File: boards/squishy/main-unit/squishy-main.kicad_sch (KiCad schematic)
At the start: 89 parts, among them J1 Conn_01x02, J3 MEM2061-01-188-00-A, J42 SU SWD, J7 SCSI PHY Mezz, J8 FLASH, J8 TRIGGER, SW2 DFU, U1 LFE5UM5G-45F-8BG381C, U18 IS66WVS4M8BLL, U19 HyperRAM, U2 GD25Q64EWIGR, U24 74AHC1G02, U6 ATSAMD09D14A-M, X1 48MHz, X3 100MHz

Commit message: squishy: main: started populating part links prior to going through each part (other than passives) and validating their footprints
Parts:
- C1, C57: OC_DIGIKEY (none) -> 399-C0402C103K3RAC7867DKR-ND; URL_DIGIKEY (none) -> https://www.digikey.com/short/n9t0571b
- C12, C47, C7: OC_DIGIKEY (none) -> 399-C0603C104M5RAC7867DKR-ND; URL_DIGIKEY (none) -> https://www.digikey.com/short/8nqzrr4b
- C13, C14, C5: OC_DIGIKEY (none) -> 587-2400-6-ND; URL_DIGIKEY (none) -> https://www.digikey.com/short/83w49wnp
- D10: OC_DIGIKEY (none) -> SMLEN3WBC8W1DKR-ND; URL_DIGIKEY (none) -> https://www.digikey.com/short/c3th3r99
- D12, D8: OC_DIGIKEY (none) -> 732-4966-6-ND; URL_DIGIKEY (none) -> https://www.digikey.com/short/ddpjpwr7
- D15: OC_DIGIKEY (none) -> 732-4978-6-ND; URL_DIGIKEY (none) -> https://www.digikey.com/short/whr1znbf
- D16: OC_DIGIKEY (none) -> 732-4980-6-ND; URL_DIGIKEY (none) -> https://www.digikey.com/short/h8jf77w9
- D17: URL_DIGIKEY (none) -> https://www.digikey.com/short/dbc27874
- J3: OC_DIGIKEY (none) -> 2073-MEM2061-01-188-00-ADKR-ND; URL_DIGIKEY (none) -> https://www.digikey.com/short/pnmr2wrw
- J42, J8: MPN FTSH-105-01-L-DV-K-TR -> FTSH-105-01-L-DV-K-P-TR; OC_DIGIKEY (none) -> 612-FTSH-105-01-L-DV-K-P-TRDKR-ND; URL_DIGIKEY (none) -> https://www.digikey.com/short/mw4tvzw7
- J7: URL_DIGIKEY (none) -> https://www.digikey.com/short/rh8jztt0
- J8: OC_DIGIKEY (none) -> WM5536-ND; URL_DIGIKEY (none) -> https://www.digikey.com/short/ch5zfdz7

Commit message: squishy: main: added the last of the Digikey order codes and URLs, some parts are not available at DigiKey and others are out of stock with long lead times, need to find alternatives. While also there are some that don't come in digireel so no idea what to do there
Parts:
- R10, R12, R37, R38, R39, R49, R58, R71, R72, R73, R74: OC_DIGIKEY (none) -> 541-4.70KHDKR-ND; URL_DIGIKEY (none) -> https://www.digikey.com/short/f3fq37nd
- R11: OC_DIGIKEY (none) -> 541-1.00MHDKR-ND; URL_DIGIKEY (none) -> https://www.digikey.com/short/18qqp0zw
- R12: OC_DIGIKEY (none) -> 541-0.0JDKR-ND; Tolerance (none) -> 1/4W; URL_DIGIKEY (none) -> https://www.digikey.com/short/qmj7b2hp
- R12: OC_DIGIKEY (none) -> 541-1.00KHDKR-ND; URL_DIGIKEY (none) -> https://www.digikey.com/short/dw9cq7z3
- R19, R20, R21, R22, R23: OC_DIGIKEY (none) -> 541-2.20KHDKR-ND; URL_DIGIKEY (none) -> https://www.digikey.com/short/bnh9rvr0
- R19, R20: OC_DIGIKEY (none) -> 541-100KHDKR-ND; URL_DIGIKEY (none) -> https://www.digikey.com/short/5n1ztv42
- R25, R3, R36, R54, R60, R64, R67, R68, R69, R70: OC_DIGIKEY (none) -> 541-10.0KHDKR-ND; URL_DIGIKEY (none) -> https://www.digikey.com/short/478v2810
- R37: OC_DIGIKEY (none) -> CAY16-4701F4LFDKR-ND; URL_DIGIKEY (none) -> https://www.digikey.com/short/zvwmjpcm
- R37, R66: OC_DIGIKEY (none) -> CAY16-103J4LFDKR-ND; URL_DIGIKEY (none) -> https://www.digikey.com/short/91vhpmq2
- R5: OC_DIGIKEY (none) -> 541-100LDKR-ND; URL_DIGIKEY (none) -> https://www.digikey.com/short/v1307zwt
- SW2: OC_DIGIKEY (none) -> SW1143DKR-ND; URL_DIGIKEY (none) -> https://www.digikey.com/short/vvt30n4j
- U1: OC_DIGIKEY (none) -> 220-2107-ND; URL_DIGIKEY (none) -> https://www.digikey.com/short/f34t0pr0
- U18, U19: OC_DIGIKEY (none) -> 448-S80KS5122GABHI020-ND; URL_DIGIKEY (none) -> https://www.digikey.com/short/rwv27n90
- U18: OC_DIGIKEY (none) -> 706-IS66WVS4M8BLL-104NLI-ND; URL_DIGIKEY (none) -> https://www.digikey.com/short/29w7cnhb
- U2: OC_DIGIKEY (none) -> 1970-GD25Q64EWIGRDKR-ND; URL_DIGIKEY (none) -> https://www.digikey.com/short/j44d557m
- U24: OC_DIGIKEY (none) -> 1727-3258-6-ND; URL_DIGIKEY (none) -> https://www.digikey.com/short/pb7573pr
- U6: OC_DIGIKEY (none) -> ATSAMD09D14A-MUTDKR-ND; URL_DIGIKEY (none) -> https://www.digikey.com/short/7423wbjd
- X1: OC_DIGIKEY (none) -> 535-ASE-48.000MHZ-L-C-TDKR-ND; URL_DIGIKEY (none) -> https://www.digikey.com/short/pmhjnqwd
- X3: OC_DIGIKEY (none) -> 535-AK3ADDF1-100.000T3DKR-ND; URL_DIGIKEY (none) -> https://www.digikey.com/short/5r299tzp

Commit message: squishy: main: BoM cleanup and alternative part selection for the ones which were out of stock
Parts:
- D11, D9: OC_DIGIKEY (none) -> OSK40603C1E; URL_DIGIKEY (none) -> https://www.tme.com/ux/en-us/details/osk40603c1e/smd-colour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
- D17: OC_DIGIKEY (none) -> 18-SP3205-01ETGCT-ND
- J7: OC_DIGIKEY (none) -> 609-5457-1-ND
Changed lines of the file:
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@@
 			)
 		)
-		(property "OC_DIGIKEY" ""
+		(property "OC_DIGIKEY" "OSK40603C1E"
 			(at 118.11 40.64 0)
 			(effects
@@
 			)
 		)
-		(property "URL_DIGIKEY" ""
+		(property "URL_DIGIKEY" "https://www.tme.com/ux/en-us/details/osk40603c1e/smd-colour-leds/optosupply/"
 			(at 118.11 40.64 0)
 			(effects
@@
 			)
 		)
-		(property "OC_DIGIKEY" ""
+		(property "OC_DIGIKEY" "OSK40603C1E"
 			(at 128.27 40.64 0)
 			(effects
@@
 			)
 		)
-		(property "URL_DIGIKEY" ""
+		(property "URL_DIGIKEY" "https://www.tme.com/ux/en-us/details/osk40603c1e/smd-colour-leds/optosupply/"
 			(at 128.27 40.64 0)
 			(effects
@@
 			)
 		)
-		(property "OC_DIGIKEY" ""
+		(property "OC_DIGIKEY" "18-SP3205-01ETGCT-ND"
 			(at 69.85 30.48 0)
 			(effects
@@
 			)
 		)
-		(property "OC_DIGIKEY" ""
+		(property "OC_DIGIKEY" "609-5457-1-ND"
 			(at 367.03 158.75 0)
 			(effects

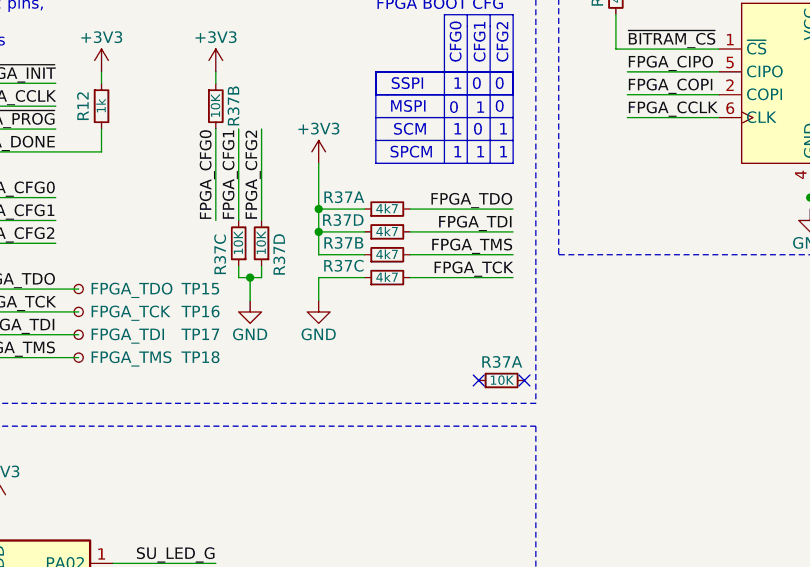
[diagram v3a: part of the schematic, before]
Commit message: squishy: main: Replaced the single 4k7 resistor network with 4 dedicated resistors to reduce BOM count
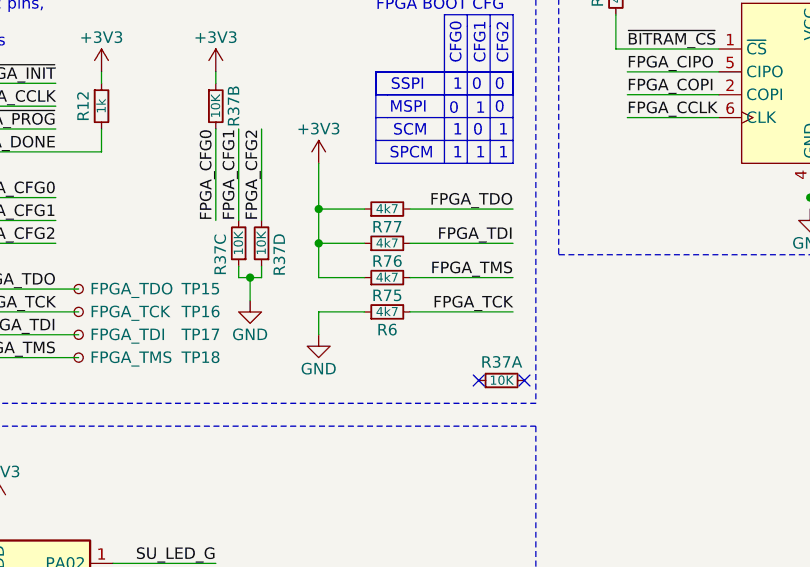
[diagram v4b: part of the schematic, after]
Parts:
- removed R37: 4k7, rhais_rcl:R0603_Array_Concave_4, symbol DX-MON:pkl_R4_Small
- added R6, R75, R76, R77: 4k7, rhais_rcl:R0603, symbol Device:R_Small
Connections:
- net +3V3: now also R75.1, R76.1, R77.1
- net FPGA_TCK: now also R6.2
- net FPGA_TDI: now also R76.2
- net FPGA_TDO: now also R77.2
- net FPGA_TMS: now also R75.2
- net GND: now also R6.1

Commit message: squishy: main: updated part fields to be more generic
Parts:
- C1, C57: OC_DIGIKEY 399-C0402C103K3RAC7867DKR-ND -> (none); SUPPLIER (none) -> DigiKey; SUPPLIER_OC (none) -> 399-C0402C103K3RAC7867DKR-ND; SUPPLIER_URL (none) -> https://www.digikey.com/short/n9t0571b; URL_DIGIKEY https://www.digikey.com/short/n9t0571b -> (none)
- C12, C47, C7: OC_DIGIKEY 399-C0603C104M5RAC7867DKR-ND -> (none); SUPPLIER (none) -> DigiKey; SUPPLIER_OC (none) -> 399-C0603C104M5RAC7867DKR-ND; SUPPLIER_URL (none) -> https://www.digikey.com/short/8nqzrr4b; URL_DIGIKEY https://www.digikey.com/short/8nqzrr4b -> (none)
- C13, C14, C5: OC_DIGIKEY 587-2400-6-ND -> (none); SUPPLIER (none) -> DigiKey; SUPPLIER_OC (none) -> 587-2400-6-ND; SUPPLIER_URL (none) -> https://www.digikey.com/short/83w49wnp; URL_DIGIKEY https://www.digikey.com/short/83w49wnp -> (none)
- D10: OC_DIGIKEY SMLEN3WBC8W1DKR-ND -> (none); SUPPLIER (none) -> DigiKey; SUPPLIER_OC (none) -> SMLEN3WBC8W1DKR-ND; SUPPLIER_URL (none) -> https://www.digikey.com/short/c3th3r99; URL_DIGIKEY https://www.digikey.com/short/c3th3r99 -> (none)
- D11, D9: OC_DIGIKEY OSK40603C1E -> (none); SUPPLIER (none) -> TME; SUPPLIER_OC (none) -> OSK40603C1E; SUPPLIER_URL (none) -> https://www.tme.com/ux/en-us/details/osk40603c1e/smd-colour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; URL_DIGIKEY https://www.tme.com/ux/en-us/details/osk40603c1e/smd-colour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 -> (none)
- D12, D8: OC_DIGIKEY 732-4966-6-ND -> (none); SUPPLIER (none) -> DigiKey; SUPPLIER_OC (none) -> 732-4966-6-ND; SUPPLIER_URL (none) -> https://www.digikey.com/short/ddpjpwr7; URL_DIGIKEY https://www.digikey.com/short/ddpjpwr7 -> (none)
- D15: OC_DIGIKEY 732-4978-6-ND -> (none); SUPPLIER (none) -> DigiKey; SUPPLIER_OC (none) -> 732-4978-6-ND; SUPPLIER_URL (none) -> https://www.digikey.com/short/whr1znbf; URL_DIGIKEY https://www.digikey.com/short/whr1znbf -> (none)
- D16: OC_DIGIKEY 732-4980-6-ND -> (none); SUPPLIER (none) -> DigiKey; SUPPLIER_OC (none) -> 732-4980-6-ND; SUPPLIER_URL (none) -> https://www.digikey.com/short/h8jf77w9; URL_DIGIKEY https://www.digikey.com/short/h8jf77w9 -> (none)
- D17: OC_DIGIKEY 18-SP3205-01ETGCT-ND -> (none); SUPPLIER (none) -> DigiKey; SUPPLIER_OC (none) -> 18-SP3205-01ETGCT-ND; SUPPLIER_URL (none) -> https://www.digikey.com/short/dbc27874; URL_DIGIKEY https://www.digikey.com/short/dbc27874 -> (none)
- J3: OC_DIGIKEY 2073-MEM2061-01-188-00-ADKR-ND -> (none); SUPPLIER (none) -> DigiKey; SUPPLIER_OC (none) -> 2073-MEM2061-01-188-00-ADKR-ND; SUPPLIER_URL (none) -> https://www.digikey.com/short/pnmr2wrw; URL_DIGIKEY https://www.digikey.com/short/pnmr2wrw -> (none)
- J42, J8: OC_DIGIKEY 612-FTSH-105-01-L-DV-K-P-TRDKR-ND -> (none); SUPPLIER_OC (none) -> 612-FTSH-105-01-L-DV-K-P-TRDKR-ND; SUPPLIER_URL (none) -> https://www.digikey.com/short/mw4tvzw7; URL_DIGIKEY https://www.digikey.com/short/mw4tvzw7 -> (none)
- J7: OC_DIGIKEY 609-5457-1-ND -> (none); SUPPLIER (none) -> DigiKey; SUPPLIER_OC (none) -> 609-5457-1-ND; SUPPLIER_URL (none) -> https://www.digikey.com/short/rh8jztt0; URL_DIGIKEY https://www.digikey.com/short/rh8jztt0 -> (none)
- J8: OC_DIGIKEY WM5536-ND -> (none); SUPPLIER_OC (none) -> WM5536-ND; SUPPLIER_URL (none) -> https://www.digikey.com/short/ch5zfdz7; URL_DIGIKEY https://www.digikey.com/short/ch5zfdz7 -> (none)
- R10, R12, R37, R38, R39, R49, R58, R6, R71, R72, R73, R74, R75, R76, R77: OC_DIGIKEY 541-4.70KHDKR-ND -> (none); SUPPLIER (none) -> DigiKey; SUPPLIER_OC (none) -> 541-4.70KHDKR-ND; SUPPLIER_URL (none) -> https://www.digikey.com/short/f3fq37nd; URL_DIGIKEY https://www.digikey.com/short/f3fq37nd -> (none)
- R11: OC_DIGIKEY 541-1.00MHDKR-ND -> (none); SUPPLIER (none) -> DigiKey; SUPPLIER_OC (none) -> 541-1.00MHDKR-ND; SUPPLIER_URL (none) -> https://www.digikey.com/short/18qqp0zw; URL_DIGIKEY https://www.digikey.com/short/18qqp0zw -> (none)
- R12: OC_DIGIKEY 541-0.0JDKR-ND -> (none); SUPPLIER (none) -> DigiKey; SUPPLIER_OC (none) -> 541-0.0JDKR-ND; SUPPLIER_URL (none) -> https://www.digikey.com/short/qmj7b2hp; URL_DIGIKEY https://www.digikey.com/short/qmj7b2hp -> (none)
- R12: OC_DIGIKEY 541-1.00KHDKR-ND -> (none); SUPPLIER (none) -> DigiKey; SUPPLIER_OC (none) -> 541-1.00KHDKR-ND; SUPPLIER_URL (none) -> https://www.digikey.com/short/dw9cq7z3; URL_DIGIKEY https://www.digikey.com/short/dw9cq7z3 -> (none)
- R19, R20, R21, R22, R23: OC_DIGIKEY 541-2.20KHDKR-ND -> (none); SUPPLIER (none) -> DigiKey; SUPPLIER_OC (none) -> 541-2.20KHDKR-ND; SUPPLIER_URL (none) -> https://www.digikey.com/short/bnh9rvr0; URL_DIGIKEY https://www.digikey.com/short/bnh9rvr0 -> (none)
- R19, R20: OC_DIGIKEY 541-100KHDKR-ND -> (none); SUPPLIER (none) -> DigiKey; SUPPLIER_OC (none) -> 541-100KHDKR-ND; SUPPLIER_URL (none) -> https://www.digikey.com/short/5n1ztv42; URL_DIGIKEY https://www.digikey.com/short/5n1ztv42 -> (none)
- R25, R3, R36, R54, R60, R64, R67, R68, R69, R70: OC_DIGIKEY 541-10.0KHDKR-ND -> (none); SUPPLIER (none) -> DigiKey; SUPPLIER_OC (none) -> 541-10.0KHDKR-ND; SUPPLIER_URL (none) -> https://www.digikey.com/short/478v2810; URL_DIGIKEY https://www.digikey.com/short/478v2810 -> (none)
- R37, R66: OC_DIGIKEY CAY16-103J4LFDKR-ND -> (none); SUPPLIER (none) -> DigiKey; SUPPLIER_OC (none) -> CAY16-103J4LFDKR-ND; SUPPLIER_URL (none) -> https://www.digikey.com/short/91vhpmq2; URL_DIGIKEY https://www.digikey.com/short/91vhpmq2 -> (none)
- R5: OC_DIGIKEY 541-100LDKR-ND -> (none); SUPPLIER (none) -> DigiKey; SUPPLIER_OC (none) -> 541-100LDKR-ND; SUPPLIER_URL (none) -> https://www.digikey.com/short/v1307zwt; URL_DIGIKEY https://www.digikey.com/short/v1307zwt -> (none)
- SW2: OC_DIGIKEY SW1143DKR-ND -> (none); SUPPLIER (none) -> DigiKey; SUPPLIER_OC (none) -> SW1143DKR-ND; SUPPLIER_URL (none) -> https://www.digikey.com/short/vvt30n4j; URL_DIGIKEY https://www.digikey.com/short/vvt30n4j -> (none)
- U1: OC_DIGIKEY 220-2107-ND -> (none); SUPPLIER (none) -> DigiKey; SUPPLIER_OC (none) -> 220-2107-ND; SUPPLIER_URL (none) -> https://www.digikey.com/short/f34t0pr0; URL_DIGIKEY https://www.digikey.com/short/f34t0pr0 -> (none)
- U18, U19: OC_DIGIKEY 448-S80KS5122GABHI020-ND -> (none); SUPPLIER (none) -> DigiKey; SUPPLIER_OC (none) -> 448-S80KS5122GABHI020-ND; SUPPLIER_URL (none) -> https://www.digikey.com/short/rwv27n90; URL_DIGIKEY https://www.digikey.com/short/rwv27n90 -> (none)
- U18: OC_DIGIKEY 706-IS66WVS4M8BLL-104NLI-ND -> (none); SUPPLIER (none) -> DigiKey; SUPPLIER_OC (none) -> 706-IS66WVS4M8BLL-104NLI-ND; SUPPLIER_URL (none) -> https://www.digikey.com/short/29w7cnhb; URL_DIGIKEY https://www.digikey.com/short/29w7cnhb -> (none)
- U2: OC_DIGIKEY 1970-GD25Q64EWIGRDKR-ND -> (none); SUPPLIER (none) -> DigiKey; SUPPLIER_OC (none) -> 1970-GD25Q64EWIGRDKR-ND; SUPPLIER_URL (none) -> https://www.digikey.com/short/j44d557m; URL_DIGIKEY https://www.digikey.com/short/j44d557m -> (none)
- U24: OC_DIGIKEY 1727-3258-6-ND -> (none); SUPPLIER (none) -> DigiKey; SUPPLIER_OC (none) -> 1727-3258-6-ND; SUPPLIER_URL (none) -> https://www.digikey.com/short/pb7573pr; URL_DIGIKEY https://www.digikey.com/short/pb7573pr -> (none)
- U6: OC_DIGIKEY ATSAMD09D14A-MUTDKR-ND -> (none); SUPPLIER (none) -> DigiKey; SUPPLIER_OC (none) -> ATSAMD09D14A-MUTDKR-ND; SUPPLIER_URL (none) -> https://www.digikey.com/short/7423wbjd; URL_DIGIKEY https://www.digikey.com/short/7423wbjd -> (none)
- X1: OC_DIGIKEY 535-ASE-48.000MHZ-L-C-TDKR-ND -> (none); SUPPLIER (none) -> DigiKey; SUPPLIER_OC (none) -> 535-ASE-48.000MHZ-L-C-TDKR-ND; SUPPLIER_URL (none) -> https://www.digikey.com/short/pmhjnqwd; URL_DIGIKEY https://www.digikey.com/short/pmhjnqwd -> (none)
- X3: OC_DIGIKEY 535-AK3ADDF1-100.000T3DKR-ND -> (none); SUPPLIER (none) -> DigiKey; SUPPLIER_OC (none) -> 535-AK3ADDF1-100.000T3DKR-ND; SUPPLIER_URL (none) -> https://www.digikey.com/short/5r299tzp; URL_DIGIKEY https://www.digikey.com/short/5r299tzp -> (none)

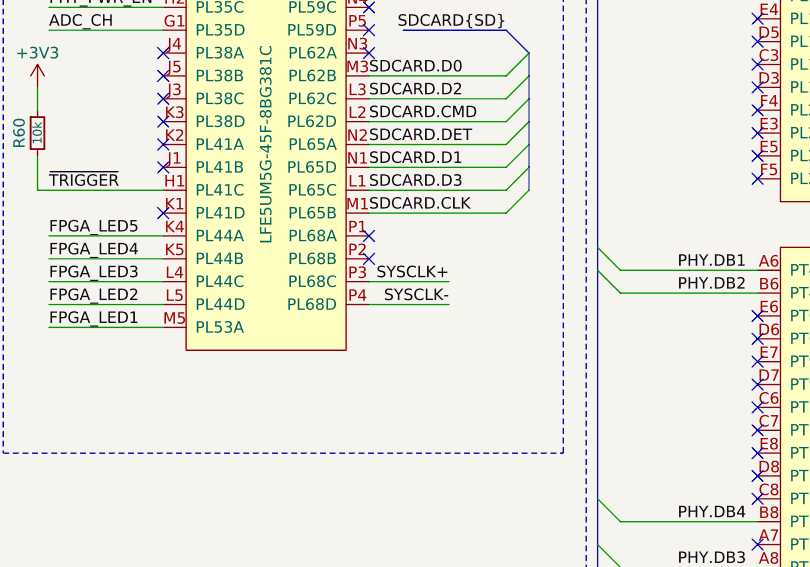
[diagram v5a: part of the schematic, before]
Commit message: squishy: main: fixed the pinout of the 100MHz and 200MHz LVDS oscillators, had to swap CLK+ and CLK- but because they're LVDS it shouldn't matter:tm:
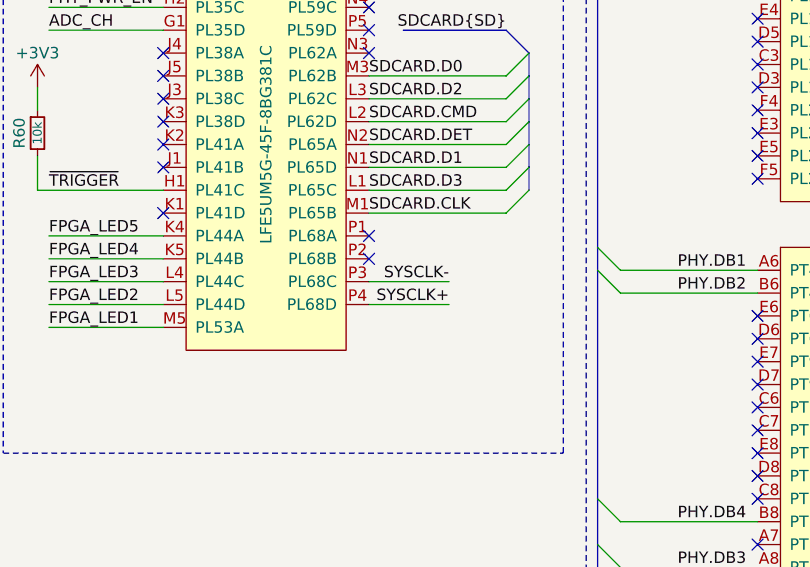
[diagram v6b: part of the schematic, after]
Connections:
- net SYSCLK+: now also U1.P4 (PL68D); no longer U1.P3 (PL68C)
- net SYSCLK-: now also U1.P3 (PL68C); no longer U1.P4 (PL68D)
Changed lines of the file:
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@@
 	(wire
 		(pts
-			(xy 241.3 146.05) (xy 250.19 146.05)
+			(xy 241.3 143.51) (xy 250.19 143.51)
 		)
 		(stroke
@@
 	(wire
 		(pts
-			(xy 241.3 143.51) (xy 250.19 143.51)
+			(xy 241.3 146.05) (xy 250.19 146.05)
 		)
 		(stroke
@@
 	)
 	(label "SYSCLK+"
-		(at 250.19 143.51 180)
+		(at 250.19 146.05 180)
 		(fields_autoplaced yes)
 		(effects
@@
 	)
 	(label "SYSCLK-"
-		(at 250.19 146.05 180)
+		(at 250.19 143.51 180)
 		(fields_autoplaced yes)
 		(effects

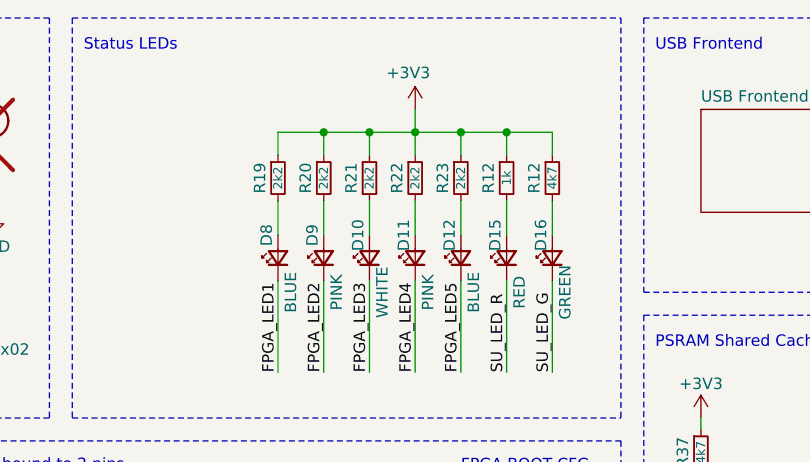
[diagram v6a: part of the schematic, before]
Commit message: squishy: main: fixed up LED values
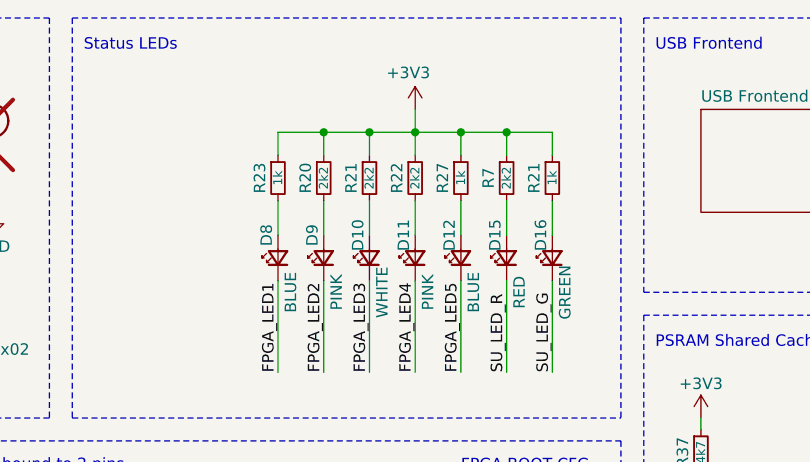
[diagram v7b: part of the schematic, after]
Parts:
- removed R12: 1k, rhais_rcl:R0603, symbol Device:R_Small
- removed R12: 4k7, rhais_rcl:R0603, symbol Device:R_Small
- removed R19: 2k2, rhais_rcl:R0603, symbol Device:R_Small
- added R21, R27: 1k, rhais_rcl:R0603, symbol Device:R_Small
- added R7: 2k2, rhais_rcl:R0603, symbol Device:R_Small
- R23: value 2k2 -> 1k; MPN CRCW06032K20FKEA -> CRCW06031K00FKEA; SUPPLIER_OC 541-2.20KHDKR-ND -> 541-1.00KHDKR-ND; SUPPLIER_URL https://www.digikey.com/short/bnh9rvr0 -> https://www.digikey.com/short/dw9cq7z3
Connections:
- net +3V3: now also R21.1, R27.1, R7.1
- net at D15.2 (A): now also R7.2
- net at D8.2 (A): now also R23.2
- net at D16.2 (A): now also R21.2
- net at D12.2 (A): now also R27.2; no longer R23.2

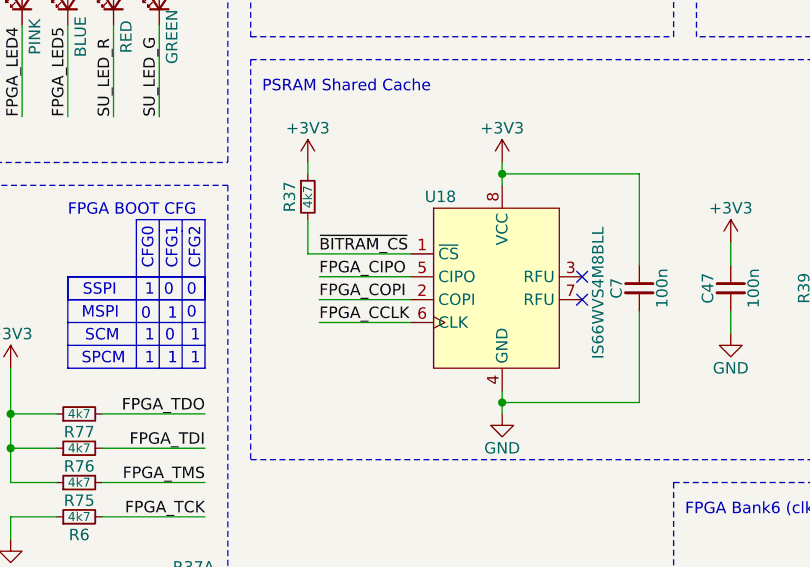
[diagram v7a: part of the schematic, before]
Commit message: squishy: main: fixed the pinout for the bitstream cache PSRAM
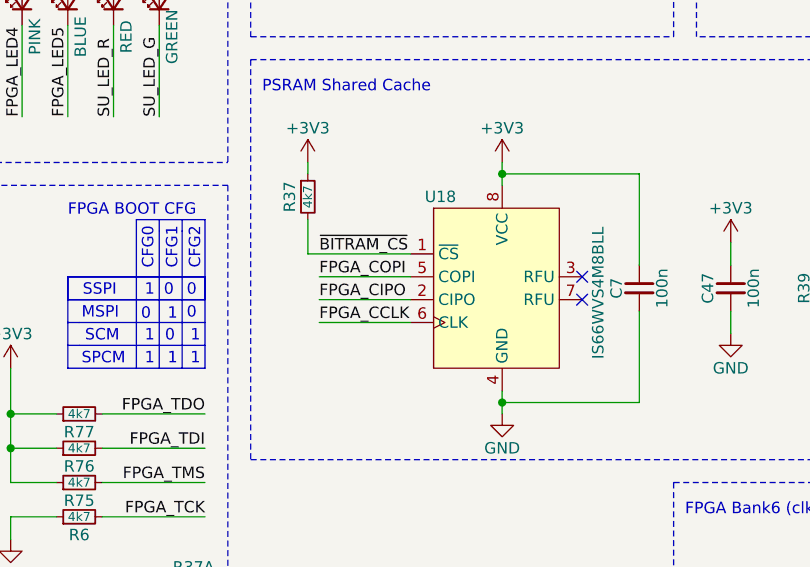
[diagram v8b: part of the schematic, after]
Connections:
- net FPGA_CIPO: now also U18.2 (CIPO); no longer U18.5 (CIPO)
- net FPGA_COPI: now also U18.5 (COPI); no longer U18.2 (COPI)
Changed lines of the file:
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@@
 	)
 	(label "FPGA_COPI"
-		(at 161.29 73.66 0)
+		(at 161.29 71.12 0)
 		(fields_autoplaced yes)
 		(effects
@@
 	)
 	(label "FPGA_CIPO"
-		(at 161.29 71.12 0)
-		(fields_autoplaced yes)
-		(effects
+		(at 161.29 73.66 0)
+		(fields_autoplaced yes)
+		(effects
